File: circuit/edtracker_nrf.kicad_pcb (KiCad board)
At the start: 2 copper layers, 50 x 44 mm, 17 parts, among them M1 NRF24LE1_SMALL, Q1 TPS1101D, SW1 SW_PUSH, SW2 SWITCH_INV, U1 NRF24LE1_PROG, U2 MPU-6050, U3 UART

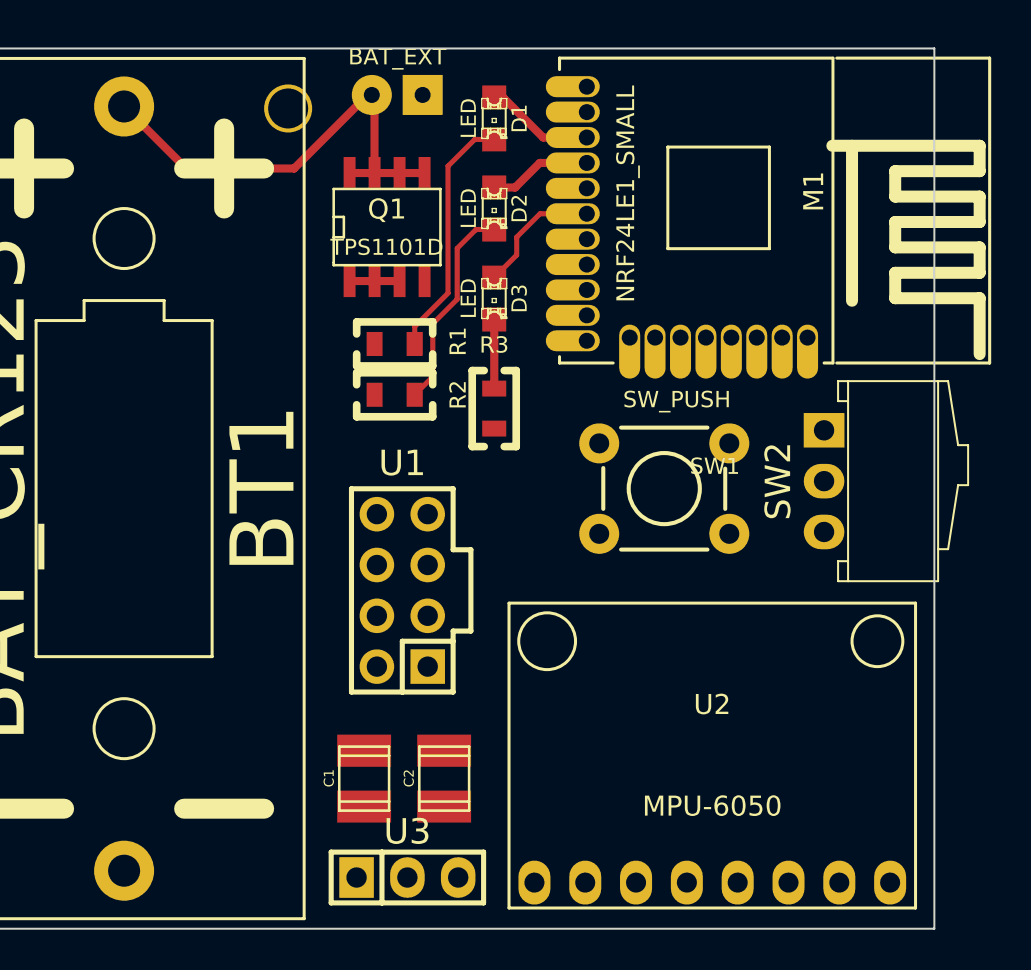
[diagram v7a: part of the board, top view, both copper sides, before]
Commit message: 
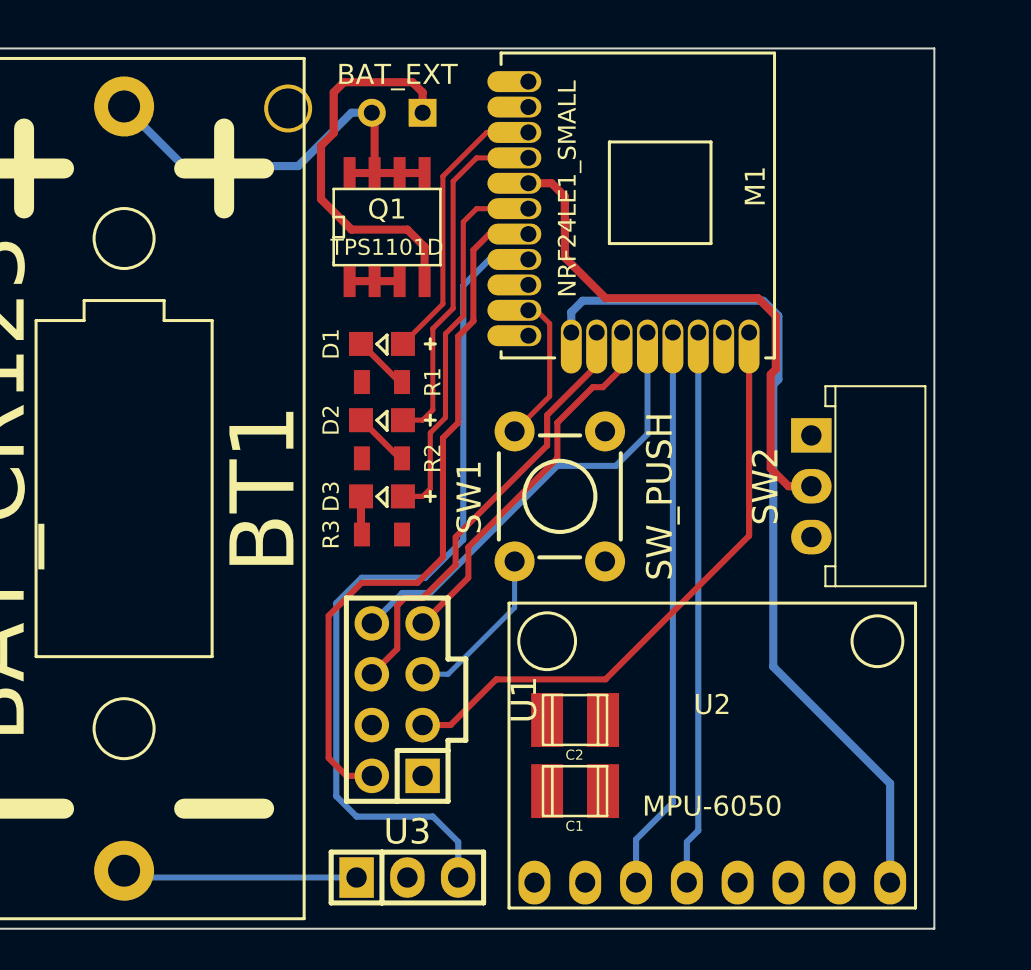
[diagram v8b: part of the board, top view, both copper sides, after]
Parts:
- D1, D2, D3: footprint LEDs:LED-0805 -> edtracker_nrf:LED-0805
- R1, R2, R3: footprint Resistors_SMD:Resistor_SMD0805_ReflowWave -> edtracker_nrf:Resistor_SMD0805_ReflowWave
- moved D1 12.6 mm to (72.4, 64.8), turned to 180 degrees
- moved D2 12.0 mm to (72.4, 68.6), turned to 180 degrees
- moved D3 11.4 mm to (72.4, 72.4), turned to 180 degrees
- moved C1 10.6 mm to (82.0, 87.1), turned to 180 degrees
- moved R3 8.43 mm to (72.4, 74.3), turned to 180 degrees
- moved C2 7.17 mm to (82.0, 83.6), turned to 180 degrees
- moved U1 5.47 mm to (73.2, 82.5)
- moved SW1 5.23 mm to (81.3, 72.4), turned to 90 degrees
- moved R2 3.24 mm to (72.4, 70.5)
- moved M1 2.93 mm to (85.3, 58.2)
- moved R1 2.01 mm to (72.4, 66.7)
- moved BT2 0.89 mm to (73.2, 53.2)
- moved SW2 0.68 mm to (93.9, 71.9)
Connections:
- net Net-(M1-Pad19) renamed /RESET
- net Net-(M1-Pad7) renamed /PROG
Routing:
- net Net-(M1-Pad12): track 0.00 -> 42.8 mm
- net Net-(M1-Pad8): track 0.00 -> 42.6 mm
- net /PROG: track 0.00 -> 35.6 mm
- net GND: track 0.00 -> 31.1 mm
- net /RESET: track 0.00 -> 30.4 mm
- net /SCL: track 0.00 -> 28.3 mm
- net /SDA: track 0.00 -> 27.7 mm
- net VCC: track 0.00 -> 27.0 mm
- net /FCSN: track 0.00 -> 24.7 mm
- net /FMOSI: track 0.00 -> 22.3 mm
- net /FMISO: track 0.00 -> 19.0 mm
- net /FSCK: track 0.00 -> 15.7 mm
- net Net-(D2-Pad1): track 5.14 -> 17.8 mm
- net Net-(D3-Pad1): track 6.73 -> 19.1 mm
- net Net-(D1-Pad2): track 12.4 -> 2.84 mm
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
